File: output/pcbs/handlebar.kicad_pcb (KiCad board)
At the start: 2 copper layers, 155.2 x 111.6 mm, 17 parts

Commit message: Nets have started working, diodes
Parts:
- added D1: , ComboDiode, F.Cu at (100.0, 105.0)
- added D10: , ComboDiode, F.Cu at (138.0, 88.0)
- added D11: , ComboDiode, F.Cu at (138.0, 71.0)
- added D12: , ComboDiode, F.Cu at (138.0, 54.0)
- added D13: , ComboDiode, F.Cu at (157.0, 105.0)
- added D14: , ComboDiode, F.Cu at (157.0, 88.0)
- added D15: , ComboDiode, F.Cu at (157.0, 71.0)
- added D16: , ComboDiode, F.Cu at (157.0, 54.0)
- added D17: , ComboDiode, F.Cu at (-38.0, -5.20)
- added D18: , ComboDiode, F.Cu at (-38.0, -22.2)
- added D19: , ComboDiode, F.Cu at (-19.0, 11.8)
- added D2: , ComboDiode, F.Cu at (100.0, 88.0)
- added D20: , ComboDiode, F.Cu at (-19.0, -5.20)
- added D21: , ComboDiode, F.Cu at (-19.0, -22.2)
- added D22: , ComboDiode, F.Cu at (132.6, 122.0)
- added D23: , ComboDiode, F.Cu at (151.6, 122.0)
- added D24: , ComboDiode, F.Cu at (177.6, 129.1)
- added D25: , ComboDiode, F.Cu at (191.1, 142.5)
- added D3: , ComboDiode, F.Cu at (100.0, 71.0)
- added D4: , ComboDiode, F.Cu at (100.0, 54.0)
- added D5: , ComboDiode, F.Cu at (119.0, 105.0)
- added D6: , ComboDiode, F.Cu at (119.0, 88.0)
- added D7: , ComboDiode, F.Cu at (119.0, 71.0)
- added D8: , ComboDiode, F.Cu at (119.0, 54.0)
- added D9: , ComboDiode, F.Cu at (138.0, 105.0)
- added S17: , PG1350, F.Cu at (-38.0, -10.2)
- added S18: , PG1350, F.Cu at (-38.0, -27.2)
- added S19: , PG1350, F.Cu at (-19.0, 6.80)
- added S20: , PG1350, F.Cu at (-19.0, -10.2)
- added S21: , PG1350, F.Cu at (-19.0, -27.2)
- added S22: , PG1350, F.Cu at (132.6, 117.0)
- added S23: , PG1350, F.Cu at (151.6, 117.0)
- added S24: , PG1350, F.Cu at (181.2, 125.5)
- added S25: , PG1350, F.Cu at (194.6, 138.9)
- moved S1 141.4 mm to (100.0, 100.0)
- moved S10 141.4 mm to (138.0, 83.0)
- moved S11 141.4 mm to (138.0, 66.0)
- moved S12 141.4 mm to (138.0, 49.0)
- moved S13 141.4 mm to (157.0, 100.0)
- moved S14 141.4 mm to (157.0, 83.0)
- moved S15 141.4 mm to (157.0, 66.0)
- moved S16 141.4 mm to (157.0, 49.0)
- moved S2 141.4 mm to (100.0, 83.0)
- moved S3 141.4 mm to (100.0, 66.0)
- moved S4 141.4 mm to (100.0, 49.0)
- moved S5 141.4 mm to (119.0, 100.0)
- moved S6 141.4 mm to (119.0, 83.0)
- moved S7 141.4 mm to (119.0, 66.0)
- moved S8 141.4 mm to (119.0, 49.0)
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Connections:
- MCU1 pad 1: net_index -> (no net)
- MCU1 pad 11: net_nums -> (no net)
- MCU1 pad 13: (no net) -> net_outer
- MCU1 pad 14: net_home -> (no net)
- MCU1 pad 15: net_top -> (no net)
- MCU1 pad 16: net_bottom -> (no net)
- MCU1 pad 2: net_middle -> (no net)
- MCU1 pad 25: (no net) -> net_inner
- MCU1 pad 26: (no net) -> net_index
- MCU1 pad 27: (no net) -> net_middle
- MCU1 pad 28: (no net) -> net_ring
- MCU1 pad 29: (no net) -> net_pinky
- MCU1 pad 5: net_ring -> net_nums
- MCU1 pad 6: (no net) -> net_top
- MCU1 pad 7: net_inner -> net_home
- MCU1 pad 8: (no net) -> net_bottom
- S1 pad 2: (no net) -> ring_bottom
- S10 pad 2: (no net) -> index_home
- S11 pad 2: (no net) -> index_top
- S12 pad 2: (no net) -> index_nums
- S13 pad 2: (no net) -> inner_bottom
- S14 pad 2: (no net) -> inner_home
- S15 pad 2: (no net) -> inner_top
- S16 pad 2: (no net) -> inner_nums
- S2 pad 2: (no net) -> ring_home
- S3 pad 2: (no net) -> ring_top
- S4 pad 2: (no net) -> ring_nums
- S5 pad 2: (no net) -> middle_bottom
- S6 pad 2: (no net) -> middle_home
- S7 pad 2: (no net) -> middle_top
- S8 pad 2: (no net) -> middle_nums
- S9 pad 2: (no net) -> index_bottom
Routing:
- net net_ring: track 0.00 -> 193.6 mm
- net (no net): track 0.00 -> 175.6 mm
- net net_middle: track 0.00 -> 172.5 mm
- net net_index: track 0.00 -> 145.8 mm
- net net_bottom: track 0.00 -> 119.6 mm
- net net_home: track 0.00 -> 104.1 mm
- net net_inner: track 0.00 -> 98.7 mm
- net net_top: track 0.00 -> 89.7 mm
- net net_nums: track 0.00 -> 76.0 mm
- net inner_home: track 0.00 -> 29.3 mm
- net center_home: track 0.00 -> 14.6 mm
- net ring_home: track 0.00 -> 14.6 mm
- net ring_bottom: track 0.00 -> 14.6 mm
- net right_home: track 0.00 -> 14.6 mm
- net middle_home: track 0.00 -> 14.6 mm
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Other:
- board size 155.2 x 111.6 mm -> 255.2 x 187.8 mm
- net class Default removed

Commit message: Board description is now decidely moving towards production. Changed Elite-C footprint for a better one. Clone the diode footprint and removed the through holes. Cloned the Choc footprint in preparation to fixing a bug in it.
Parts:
- removed MCU1: Elite-C-castellated-29pin-holes, Elite-C-castellated-29pin-holes
- added ?: , elite-c, F.Cu at (182.9, 60.0)
- moved D17 142.8 mm to (64.0, 94.8)
- moved D18 142.8 mm to (64.0, 77.8)
- moved S17 142.8 mm to (64.0, 89.8)
- moved S18 142.8 mm to (64.0, 72.8)
- moved D19 142.1 mm to (82.0, 111.8)
- moved D20 142.1 mm to (82.0, 94.8)
- moved D21 142.1 mm to (82.0, 77.8)
- moved S19 142.1 mm to (82.0, 106.8)
- moved S20 142.1 mm to (82.0, 89.8)
- moved S21 142.1 mm to (82.0, 72.8)
- moved S25 7.65 mm to (192.7, 131.5)
- moved D24 7.65 mm to (175.7, 121.6)
- moved S24 7.65 mm to (179.3, 118.1)
- moved D25 7.65 mm to (189.2, 135.1)
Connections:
- net center_home renamed center_thumb
- net left_home renamed left_thumb
- net right_home renamed right_thumb
- net tip_home renamed outer_home
- net tip_top renamed outer_top
- D17 pad 1: (no net) -> net_home
- D18 pad 1: (no net) -> net_top
- D19 pad 1: (no net) -> net_bottom
- D20 pad 1: (no net) -> net_home
- D21 pad 1: (no net) -> net_top
- D22 pad 1: (no net) -> net_thumb
- D23 pad 1: (no net) -> net_thumb
- D24 pad 1: (no net) -> net_thumb
- D25 pad 1: (no net) -> net_thumb
- D25 pad 2: inner_home -> inner_thumb
- S17 pad 1: (no net) -> net_outer
- S18 pad 1: (no net) -> net_outer
- S19 pad 1: (no net) -> net_pinky
- S20 pad 1: (no net) -> net_pinky
- S21 pad 1: (no net) -> net_pinky
- S22 pad 1: (no net) -> net_ring
- S23 pad 1: (no net) -> net_middle
- S24 pad 1: (no net) -> net_index
- S25 pad 1: (no net) -> net_inner
- S25 pad 2: inner_home -> inner_thumb
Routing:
- net net_ring: track 193.6 -> 0.00 mm
- net net_middle: track 172.5 -> 0.00 mm
- net (no net): track 175.6 -> 342.9 mm
- net net_index: track 145.8 -> 0.00 mm
- net net_bottom: track 119.6 -> 0.00 mm
- net net_home: track 104.1 -> 0.00 mm
- net net_inner: track 98.7 -> 0.00 mm
- net net_top: track 89.7 -> 0.00 mm
- net net_nums: track 76.0 -> 0.00 mm
- net inner_home: track 29.3 -> 0.00 mm
- net center_thumb: track 14.6 -> 0.00 mm
- net ring_home: track 14.6 -> 0.00 mm
- net ring_bottom: track 14.6 -> 0.00 mm
- net right_thumb: track 14.6 -> 0.00 mm
- net middle_home: track 14.6 -> 0.00 mm
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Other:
- board size 255.2 x 187.8 mm -> 153.6 x 106.8 mm
- net class Default added: clearance 0.2, trace_width 0.25, via_dia 0.8, via_drill 0.4

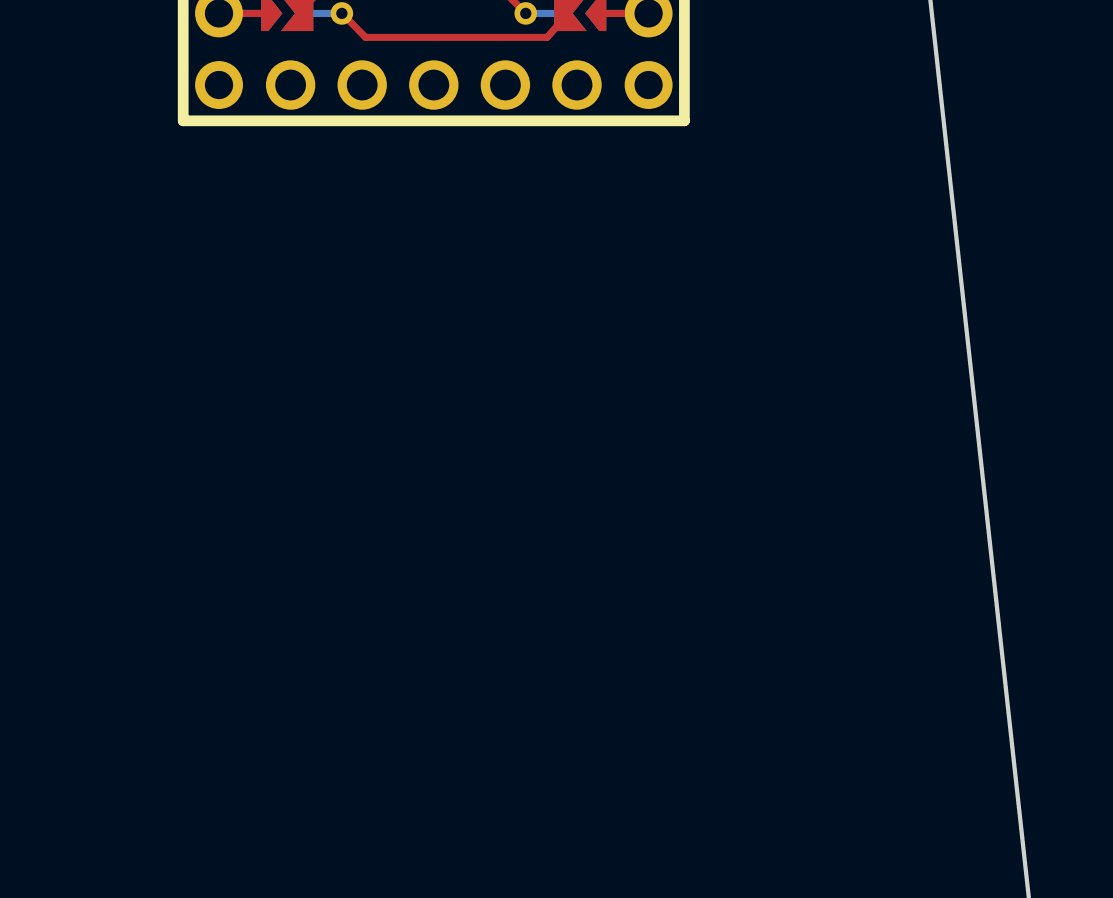
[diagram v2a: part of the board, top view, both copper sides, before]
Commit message: Added the reset button, TRRS and two indicator RGB LEDs.
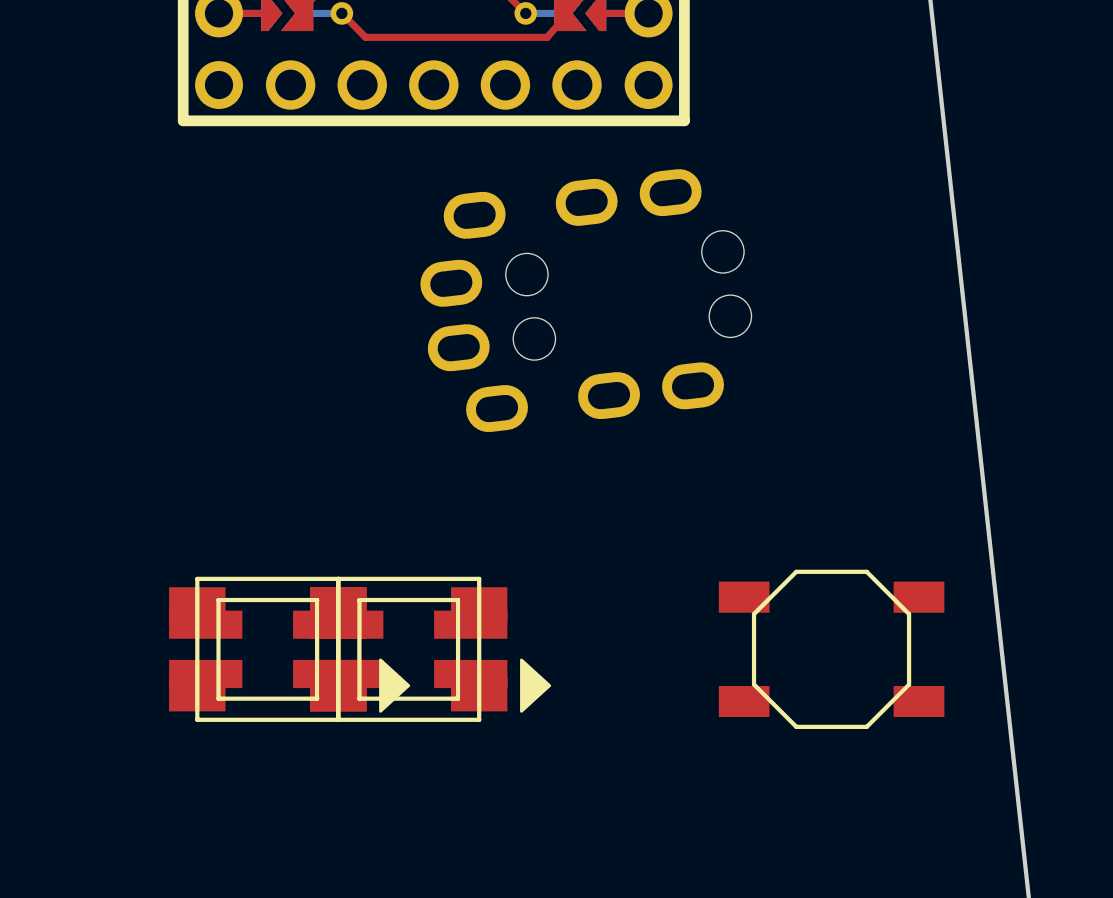
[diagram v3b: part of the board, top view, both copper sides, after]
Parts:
- added B1: , E73:SW_TACT_ALPS_SKQGABE010, F.Cu at (197.0, 94.0)
- added I1: , WS2812B, F.Cu at (177.0, 94.0)
- added I2: , WS2812B, F.Cu at (182.0, 94.0)
- added TRRS1: TRRS-PJ-320A-dual, TRRS-PJ-320A-dual, F.Cu at (195.0, 82.0)

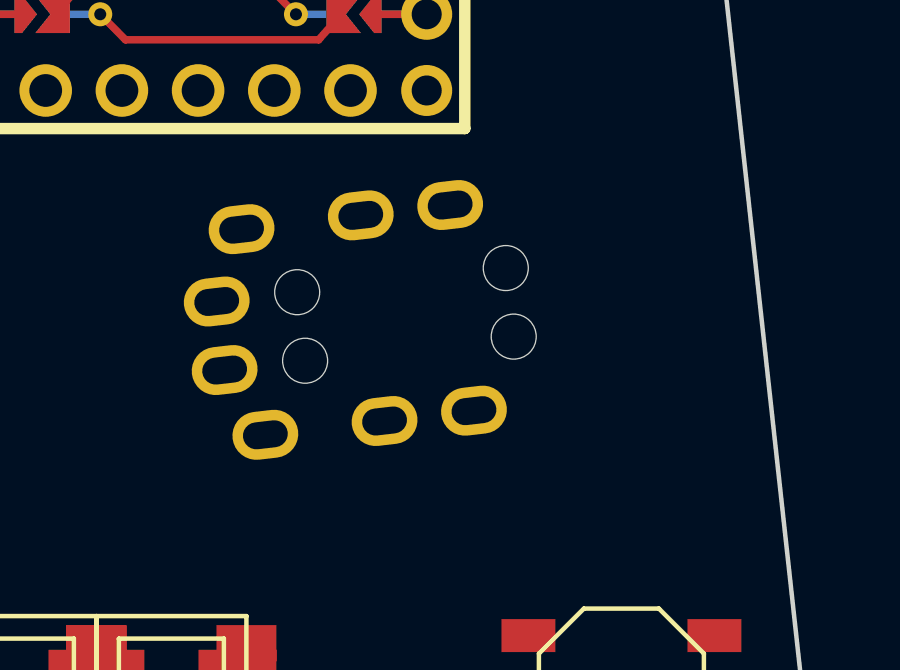
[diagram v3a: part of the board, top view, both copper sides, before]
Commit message: Adjust TRRS position
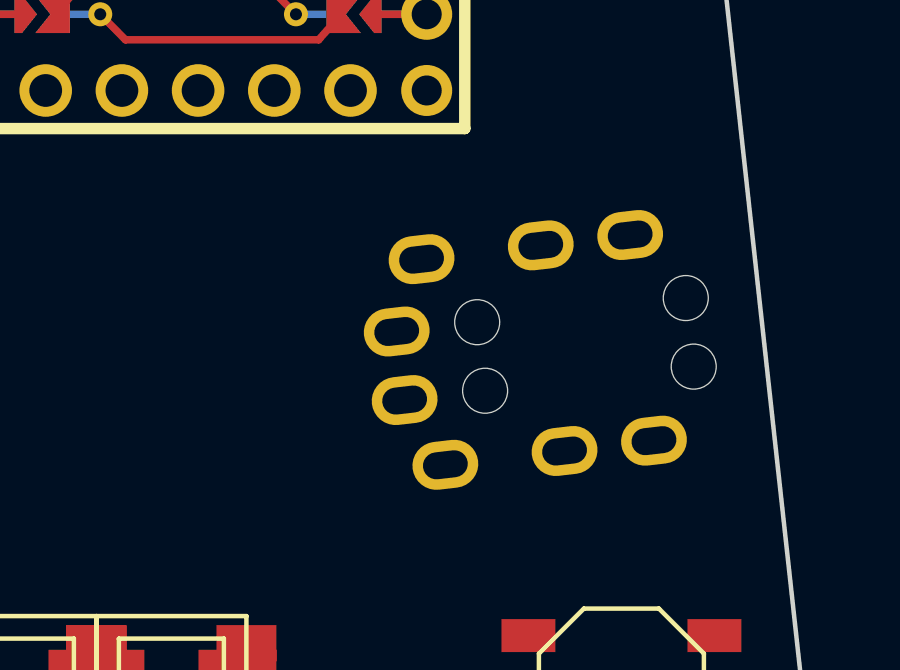
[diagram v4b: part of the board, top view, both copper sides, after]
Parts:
- moved TRRS1 6.08 mm to (201.0, 83.0)
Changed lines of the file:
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@@
     )
       (module TRRS-PJ-320A-dual (layer F.Cu)
-      (at 195 82 -83.4)
+      (at 201 83 -83.4)
       (fp_text reference "TRRS1" (at 0 14.2) (layer Dwgs.User) (effects (font (size 1 1) (thickness 0.15))))
       (fp_text value TRRS-PJ-320A-dual (at 0 -5.6) (layer F.Fab) (effects (font (size 1 1) (thickness 0.15))))

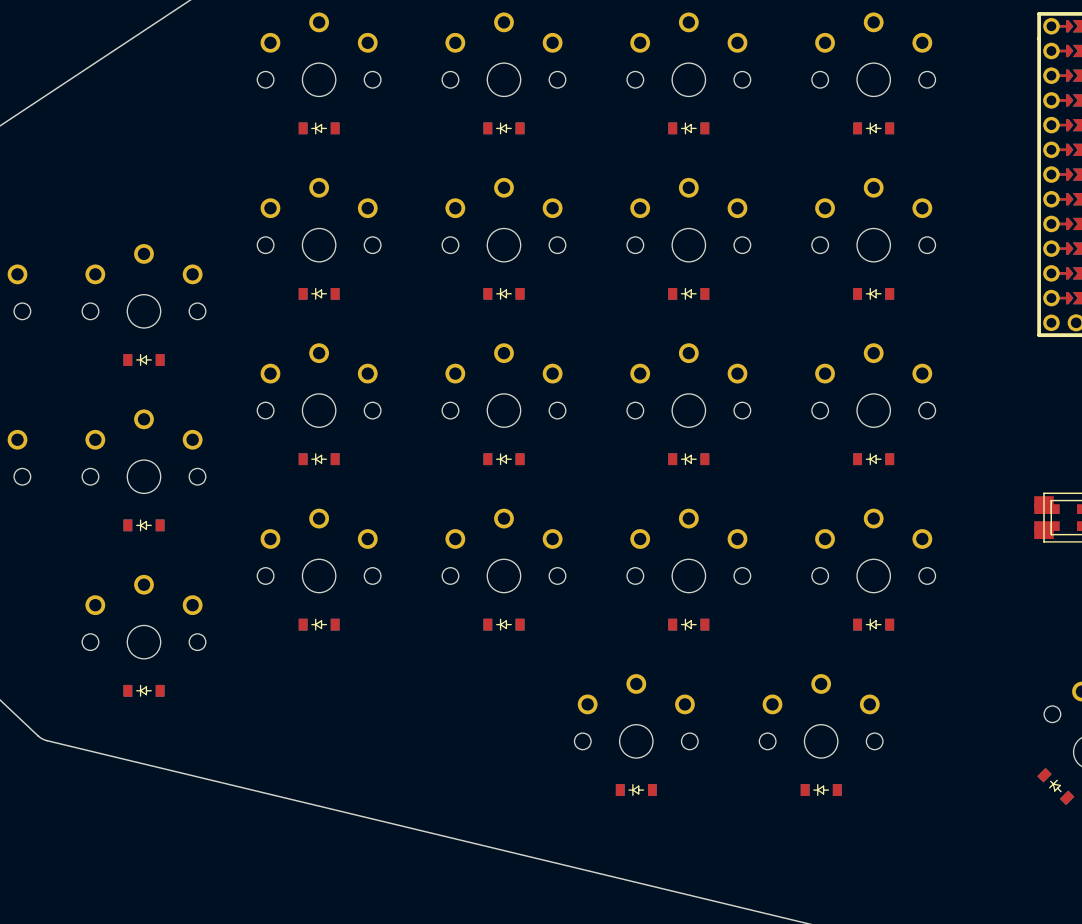
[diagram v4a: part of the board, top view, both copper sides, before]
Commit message: Add mounting holes
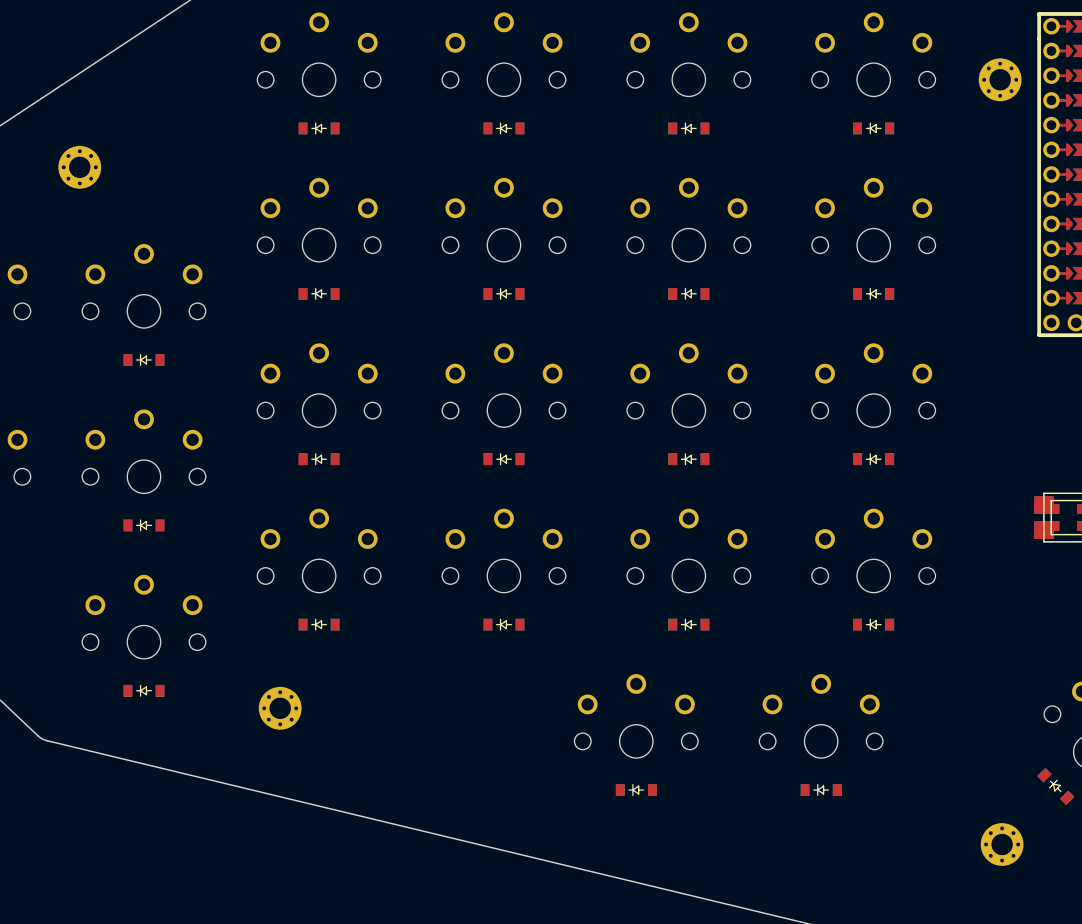
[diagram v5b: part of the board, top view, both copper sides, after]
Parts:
- added _2: , MountingHole_2.2mm_M2_Pad_Via, F.Cu at (75.4, 58.0)
- added _3: , MountingHole_2.2mm_M2_Pad_Via, F.Cu at (96.0, 113.6)
- added _4: , MountingHole_2.2mm_M2_Pad_Via, F.Cu at (170.0, 49.0)
- added _5: , MountingHole_2.2mm_M2_Pad_Via, F.Cu at (170.2, 127.6)

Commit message: Board description is now decidely moving towards production. Changed Elite-C footprint for a better one. Clone the diode footprint and removed the through holes. Cloned the Choc footprint in preparation to fixing a bug in it. Added space for the I2C pullup resistors.
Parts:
- moved I2 2.30 mm to (184.3, 94.0), turned to 90 degrees
- turned I1 to 90 degrees
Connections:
- ? pad 10: E6 -> n_bottom
- ? pad 11: B4 -> n_thumb
- ? pad 12: B5 -> n_inner
- ? pad 13: net_outer -> n_index
- ? pad 25: _1_25 -> VBUS
- ? pad 26: net_pinky -> F0
- ? pad 27: net_ring -> F1
- ? pad 28: net_middle -> C7
- ? pad 29: net_index -> D5
- ? pad 3: GND -> n_gnd
- ? pad 30: net_inner -> B7
- ? pad 4: GND -> n_gnd
- ? pad 5: net_nums -> n_sda
- ? pad 6: net_top -> n_scl
- ? pad 7: net_home -> n_nums
- ? pad 8: net_bottom -> n_top
- ? pad 9: net_thumb -> n_home
- B1 pad 1: (no net) -> n_reset
- B1 pad 2: (no net) -> n_gnd
- D1 pad 1: net_bottom -> n_bottom
- D10 pad 1: net_home -> n_home
- D11 pad 1: net_top -> n_top
- D12 pad 1: net_nums -> n_nums
- D13 pad 1: net_bottom -> n_bottom
- D14 pad 1: net_home -> n_home
- D15 pad 1: net_top -> n_top
- D16 pad 1: net_nums -> n_nums
- D17 pad 1: net_home -> n_home
- D18 pad 1: net_top -> n_top
- D19 pad 1: net_bottom -> n_bottom
- D2 pad 1: net_home -> n_home
- D20 pad 1: net_home -> n_home
- D21 pad 1: net_top -> n_top
- D22 pad 1: net_thumb -> n_thumb
- D23 pad 1: net_thumb -> n_thumb
- D24 pad 1: net_thumb -> n_thumb
- D25 pad 1: net_thumb -> n_thumb
- D3 pad 1: net_top -> n_top
- D4 pad 1: net_nums -> n_nums
- D5 pad 1: net_bottom -> n_bottom
- D6 pad 1: net_home -> n_home
- D7 pad 1: net_top -> n_top
- D8 pad 1: net_nums -> n_nums
- D9 pad 1: net_bottom -> n_bottom
- I1 pad 1: (no net) -> n_vcc
- I1 pad 11: (no net) -> n_vcc
- I1 pad 2: (no net) -> n_indic_next
- I1 pad 22: (no net) -> n_indic_next
- I1 pad 3: (no net) -> n_gnd
- I1 pad 33: (no net) -> n_gnd
- I1 pad 4: (no net) -> n_indic
- I1 pad 44: (no net) -> n_indic
- I2 pad 1: (no net) -> n_vcc
- I2 pad 11: (no net) -> n_vcc
- I2 pad 3: (no net) -> n_gnd
- I2 pad 33: (no net) -> n_gnd
- I2 pad 4: (no net) -> n_indic_next
- I2 pad 44: (no net) -> n_indic_next
- S1 pad 1: net_ring -> n_ring
- S10 pad 1: net_index -> n_index
- S11 pad 1: net_index -> n_index
- S12 pad 1: net_index -> n_index
- S13 pad 1: net_inner -> n_inner
- S14 pad 1: net_inner -> n_inner
- S15 pad 1: net_inner -> n_inner
- S16 pad 1: net_inner -> n_inner
- S17 pad 1: net_outer -> n_outer
- S18 pad 1: net_outer -> n_outer
- S19 pad 1: net_pinky -> n_pinky
- S2 pad 1: net_ring -> n_ring
- S20 pad 1: net_pinky -> n_pinky
- S21 pad 1: net_pinky -> n_pinky
- S22 pad 1: net_ring -> n_ring
- S23 pad 1: net_middle -> n_middle
- S24 pad 1: net_index -> n_index
- S25 pad 1: net_inner -> n_inner
- S3 pad 1: net_ring -> n_ring
- S4 pad 1: net_ring -> n_ring
- S5 pad 1: net_middle -> n_middle
- S6 pad 1: net_middle -> n_middle
- S7 pad 1: net_middle -> n_middle
- S8 pad 1: net_middle -> n_middle
- S9 pad 1: net_index -> n_index
- TRRS1 pad 1: (no net) -> n_gnd
- TRRS1 pad 2: (no net) -> n_sda
- TRRS1 pad 3: (no net) -> n_scl
- TRRS1 pad 4: (no net) -> n_vcc
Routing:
- net (no net): track 342.9 -> 11.1 mm
- net n_ring: track 0.00 -> 265.2 mm
- net n_middle: track 0.00 -> 248.0 mm
- net n_index: track 0.00 -> 235.9 mm
- net n_pinky: track 0.00 -> 228.5 mm
- net n_outer: track 0.00 -> 204.0 mm
- net n_inner: track 0.00 -> 179.6 mm
- net n_home: track 0.00 -> 143.8 mm
- net n_bottom: track 0.00 -> 139.7 mm
- net n_top: track 0.00 -> 138.2 mm, vias 0 -> 2
- net n_thumb: track 0.00 -> 128.5 mm
- net n_nums: track 0.00 -> 99.2 mm, vias 0 -> 2
- net n_vcc: track 0.00 -> 88.2 mm
- net n_reset: track 0.00 -> 67.6 mm
- net n_scl: track 0.00 -> 57.0 mm
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- added copper zone on F.Cu, net n_gnd
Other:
- net class Default removed
